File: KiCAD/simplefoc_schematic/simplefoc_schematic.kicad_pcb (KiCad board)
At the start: 2 copper layers, 51.9 x 74.3 mm, 67 parts, among them IC1 TMC6140-Trinamic, J1 Power Supply, J2 Motor Connector, J3 Sensor Connector, J5 Programming Port, J6 UART Port, J7 Conn_01x03, Q1 IRLR 2905, Q2 IRLR 2905, Q3 IRLR 2905, Q4 IRLR 2905, Q5 IRLR 2905, Q6 IRLR 2905, SW1 SW_Push, U2 STM32F101CBT6, Y1 8MHz

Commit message: Removed unused components and replaced some components with smaller ones
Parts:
- removed C21: 10uF/35V, Capacitor_SMD:CP_Elec_4x5.8
- removed C32: 100nF/35V, Capacitor_SMD:C_0603_1608Metric
- removed C33: 10uF/6.3V, Capacitor_SMD:C_0603_1608Metric
- removed D3: D_Schottky, Diode_SMD:D_SMA
- removed R13: 47k, Resistor_SMD:R_0603_1608Metric
- removed Y1: 8MHz, Crystal:Crystal_SMD_HC49-SD
- added U1: MC7805CDTG, Package_TO_SOT_SMD:TO-252-2, F.Cu at (254.9, 59.2)
- C12: value 100nF/35V -> 10uF/35V; moved to F.Cu
- C13: value 20pF/6V -> 10uF/35V; moved to F.Cu
- C14, C16: footprint Capacitor_SMD:CP_Elec_4x5.8 -> Capacitor_SMD:C_0603_1608Metric
- C18: value 20pF/6V -> 100nF/35V; moved to F.Cu
- C19: footprint Capacitor_SMD:CP_Elec_4x5.8 -> Capacitor_SMD:C_0603_1608Metric; moved to F.Cu
- C25, C26: value 10uF/6.3V -> 22uF/6.3V
- D1, D2: footprint Diode_SMD:D_SMA -> Additional_Components:DIODE_MSS1P4-M3_89A
- J7: value Conn_01x03 -> Servo
- R10: value 1mOhm/3W -> 0R; footprint Resistor_SMD:R_2512_6332Metric -> Resistor_SMD:R_0603_1608Metric; moved to F.Cu
- R12: value 47k -> 22k
- R7: value FBead -> 10k; footprint Resistor_SMD:R_0805_2012Metric -> Resistor_SMD:R_0603_1608Metric
- R8, R9: value 1mOhm/3W -> 10k; footprint Resistor_SMD:R_2512_6332Metric -> Resistor_SMD:R_0603_1608Metric
- moved R10 65.5 mm to (254.8, 26.8), turned to 0 degrees
- moved C19 33.2 mm to (262.9, 56.5), turned to 0 degrees
- moved C18 31.3 mm to (262.9, 59.0), turned to 0 degrees
- moved C13 20.6 mm to (278.5, 72.5), turned to 0 degrees
- moved C12 20.1 mm to (274.5, 72.5), turned to 0 degrees
- moved D1 10.2 mm to (247.0, 23.8)
- moved Q2 5.68 mm to (191.5, 80.2)
- moved Q4 5.68 mm to (191.5, 72.1)
- moved Q6 5.68 mm to (191.6, 87.4)
- moved Q1 5.68 mm to (203.6, 80.2)
- moved Q3 5.68 mm to (203.7, 87.5)
- moved Q5 5.68 mm to (203.6, 72.1)
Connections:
- C12 pad 1: +3.3V -> GND
- C12 pad 2: GND -> Net-(IC1-Pad33)
- C13 pad 1: GND -> +BATT
- C13 pad 2: Net-(C13-Pad2) -> GND
- C14 pad 1: Net-(C14-Pad1) -> +BATT
- C16 pad 1: GND -> +BATT
- C16 pad 2: +BATT -> GND
- C18 pad 2: Net-(C18-Pad2) -> +BATT
- C19 pad 1: GND -> +5V
- C19 pad 2: +BATT -> GND
- C3 pad 1: Net-(C3-Pad1) -> +3.3V
- C5 pad 1: Net-(C3-Pad1) -> +3.3V
- IC1 pad 10: Net-(C22-Pad2) -> Net-(IC1-Pad10)
- IC1 pad 22: CURRU -> unconnected-(IC1-Pad22)
- IC1 pad 23: CURRV -> unconnected-(IC1-Pad23)
- IC1 pad 25: CURRW -> unconnected-(IC1-Pad25)
- IC1 pad 26: SensU -> GND
- IC1 pad 27: SensV -> GND
- IC1 pad 28: SensW -> GND
- IC1 pad 29: DRV_STRENGTH -> unconnected-(IC1-Pad29)
- IC1 pad 30: GAIN -> unconnected-(IC1-Pad30)
- IC1 pad 33: Net-(C14-Pad1) -> Net-(IC1-Pad33)
- J3 pad 5: Thermo -> unconnected-(J3-Pad5)
- J3 pad 6: +5V -> +3.3V
- L1 pad 2: Net-(C22-Pad2) -> Net-(IC1-Pad10)
- Q4 pad 3: SensU -> GND
- Q5 pad 3: SensV -> GND
- Q6 pad 3: SensW -> GND
- R10 pad 1: SensW -> Net-(IC1-Pad10)
- R10 pad 2: GND -> Net-(C22-Pad2)
- R12 pad 1: BRAKE-0 -> Net-(IC1-Pad19)
- R12 pad 2: Net-(IC1-Pad19) -> +3.3V
- R7 pad 2: Net-(C3-Pad1) -> ENCA
- R8 pad 1: SensV -> +3.3V
- R8 pad 2: GND -> ENCB
- R9 pad 1: SensU -> +3.3V
- R9 pad 2: GND -> ENCC
- U2 pad 10: unconnected-(U2-Pad10) -> Servo
- U2 pad 11: HO1 -> unconnected-(U2-Pad11)
- U2 pad 12: LO1 -> unconnected-(U2-Pad12)
- U2 pad 13: HO2 -> DIAG
- U2 pad 14: LO2 -> unconnected-(U2-Pad14)
- U2 pad 15: HO3 -> ENABLE
- U2 pad 16: LO3 -> unconnected-(U2-Pad16)
- U2 pad 17: CURRW -> ENCC
- U2 pad 18: CURRU -> ENCB
- U2 pad 19: CURRV -> ENCA
- U2 pad 25: ENCA -> unconnected-(U2-Pad25)
- U2 pad 26: ENCB -> LO1
- U2 pad 27: ENCC -> LO2
- U2 pad 28: unconnected-(U2-Pad28) -> LO3
- U2 pad 29: unconnected-(U2-Pad29) -> HO1
- U2 pad 30: unconnected-(U2-Pad30) -> HO2
- U2 pad 31: unconnected-(U2-Pad31) -> HO3
- U2 pad 42: unconnected-(U2-Pad42) -> TX
- U2 pad 43: unconnected-(U2-Pad43) -> RX
- U2 pad 5: Net-(C13-Pad2) -> unconnected-(U2-Pad5)
- U2 pad 6: Net-(C18-Pad2) -> unconnected-(U2-Pad6)
- U2 pad 9: Net-(C3-Pad1) -> +3.3V

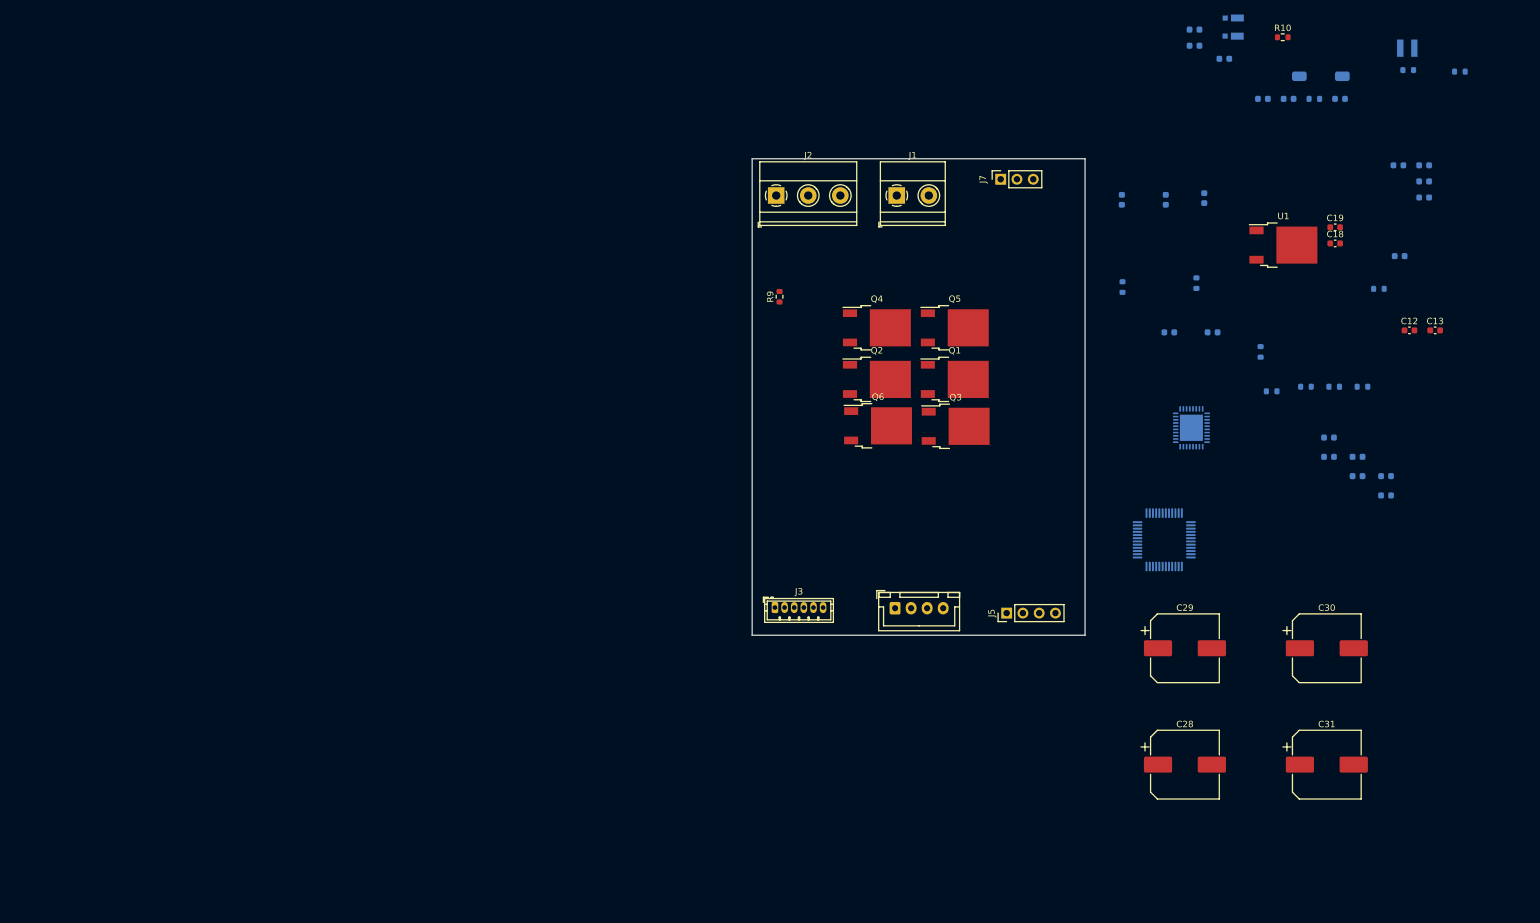
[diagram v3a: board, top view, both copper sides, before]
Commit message: Created first board layout for test board
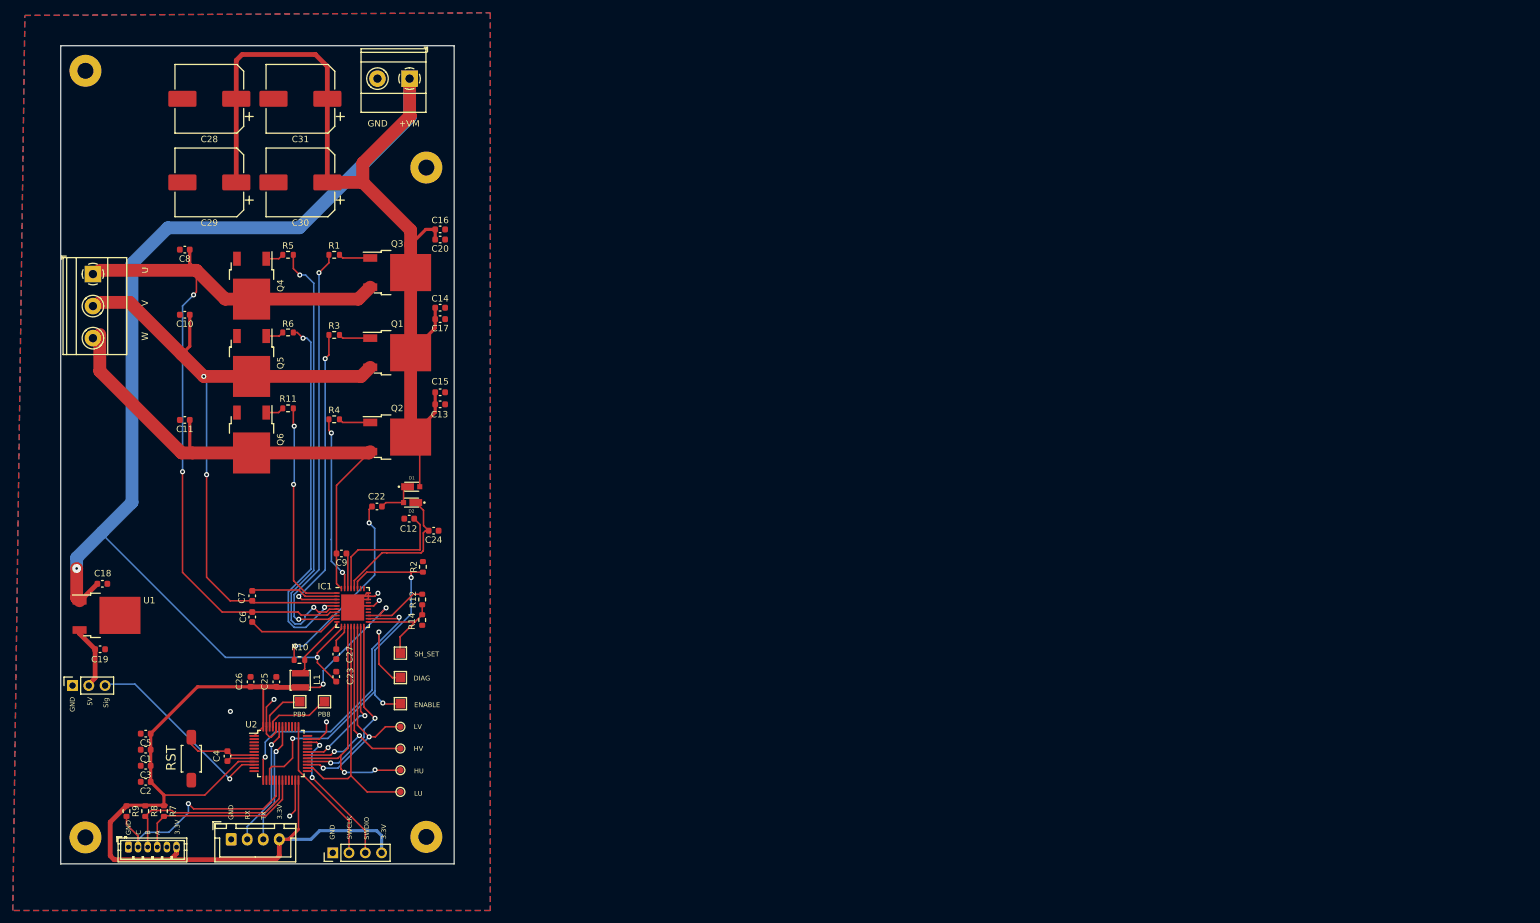
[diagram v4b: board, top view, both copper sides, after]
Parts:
- added H1: MountingHole_Pad, MountingHole:MountingHole_2.5mm_Pad, F.Cu at (121.2, 47.1)
- added H2: MountingHole_Pad, MountingHole:MountingHole_2.5mm_Pad, F.Cu at (68.0, 151.6)
- added H3: MountingHole_Pad, MountingHole:MountingHole_2.5mm_Pad, F.Cu at (68.0, 32.1)
- added H4: MountingHole_Pad, MountingHole:MountingHole_2.5mm_Pad, F.Cu at (121.2, 151.5)
- added TP1: TestPoint, TestPoint:TestPoint_Pad_1.5x1.5mm, F.Cu at (117.1, 122.9)
- added TP2: TestPoint, TestPoint:TestPoint_Pad_1.5x1.5mm, F.Cu at (117.1, 130.8)
- added TP3: TestPoint, TestPoint:TestPoint_Pad_D1.0mm, F.Cu at (117.1, 141.1)
- added TP4: TestPoint, TestPoint:TestPoint_Pad_1.5x1.5mm, F.Cu at (117.1, 126.7)
- added TP5: TestPoint, TestPoint:TestPoint_Pad_1.5x1.5mm, F.Cu at (101.4, 130.5)
- added TP6: TestPoint, TestPoint:TestPoint_Pad_1.5x1.5mm, F.Cu at (105.3, 130.5)
- added TP7: TestPoint, TestPoint:TestPoint_Pad_D1.0mm, F.Cu at (117.1, 144.5)
- added TP8: TestPoint, TestPoint:TestPoint_Pad_D1.0mm, F.Cu at (117.1, 137.8)
- added TP9: TestPoint, TestPoint:TestPoint_Pad_D1.0mm, F.Cu at (117.1, 134.4)
- C1, C10, C11, C14, C15, C16, C17, C2, C20, C22, C23, C24, C25, C26, C27, C3, C4, C5, C6, C7, C8, C9, D1, D2, IC1, L1, R1, R11, R12, R14, R2, R3, R4, R5, R6, R7, R8, SW1, U2: moved to F.Cu
- moved C5 216.2 mm to (77.4, 135.4)
- moved C2 212.1 mm to (77.4, 143.0)
- moved R8 209.0 mm to (77.3, 147.5), turned to -90 degrees
- moved SW1 205.8 mm to (84.5, 139.3), turned to 90 degrees
- moved C19 203.6 mm to (70.3, 122.3)
- moved C18 199.5 mm to (70.7, 112.1), turned to 180 degrees
- moved L1 198.8 mm to (101.5, 127.1), turned to 90 degrees
- moved C10 194.7 mm to (83.5, 70.1)
- moved C11 193.4 mm to (83.5, 86.5)
- moved C26 192.7 mm to (93.8, 127.4), turned to -90 degrees
- moved U1 192.4 mm to (71.3, 117.0)
- moved C31 190.8 mm to (101.5, 36.4), turned to 180 degrees
- moved R7 184.8 mm to (80.3, 147.5), turned to -90 degrees
- moved C28 184.2 mm to (87.3, 36.4), turned to 180 degrees
- moved R14 183.1 mm to (120.5, 117.7), turned to 90 degrees
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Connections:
- net Net-(IC1-Pad19) renamed SH_SET
- J1 pad 1: GND -> +BATT
- J1 pad 2: +BATT -> GND
- J2 pad 1: W -> U
- J2 pad 3: U -> W
- U2 pad 45: unconnected-(U2-Pad45) -> PB8
- U2 pad 46: unconnected-(U2-Pad46) -> PB9
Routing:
- net +BATT: track 0.00 -> 323.4 mm, vias 0 -> 2
- net +3.3V: track 0.00 -> 171.9 mm, vias 0 -> 2
- net U: track 0.00 -> 123.5 mm, vias 0 -> 2
- net V: track 0.00 -> 107.7 mm, vias 0 -> 2
- net W: track 0.00 -> 82.4 mm
- net LOUTU: track 0.00 -> 69.6 mm, vias 0 -> 2
- net HOUTU: track 0.00 -> 65.8 mm, vias 0 -> 2
- net ENABLE: track 0.00 -> 63.0 mm, vias 0 -> 3
- net LOUTV: track 0.00 -> 57.9 mm, vias 0 -> 2
- net DIAG: track 0.00 -> 56.2 mm, vias 0 -> 3
- net HOUTV: track 0.00 -> 48.9 mm, vias 0 -> 2
- net GND: track 0.00 -> 40.8 mm, vias 0 -> 6
- net LO1: track 0.00 -> 39.7 mm
- net HO1: track 0.00 -> 37.8 mm, vias 0 -> 2
- net LO2: track 0.00 -> 35.4 mm, vias 0 -> 2
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- added copper zone on B.Cu, net GND
- added copper zone on F.Cu, net GND
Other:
- board size 51.9 x 74.3 mm -> 61.4 x 127.6 mm
- board text added: "+VM"
- board text added: "3.3V"
- board text added: "5V"
- board text added: "A"
- board text added: "B"
- board text added: "C"
- board text added: "DIAG"
- board text added: "ENABLE"
- board text added: "GND"
- board text added: "HU"
- board text added: "HV"
- board text added: "LU"
- board text added: "LV"
- board text added: "PB8"
- board text added: "PB9"
- board text added: "RST"
- board text added: "RX"
- board text added: "SH_SET"
- board text added: "SWCLK"
- board text added: "SWDIO"
- board text added: "Sig"
- board text added: "TX"
- board text added: "U"
- board text added: "V"
- board text added: "W"

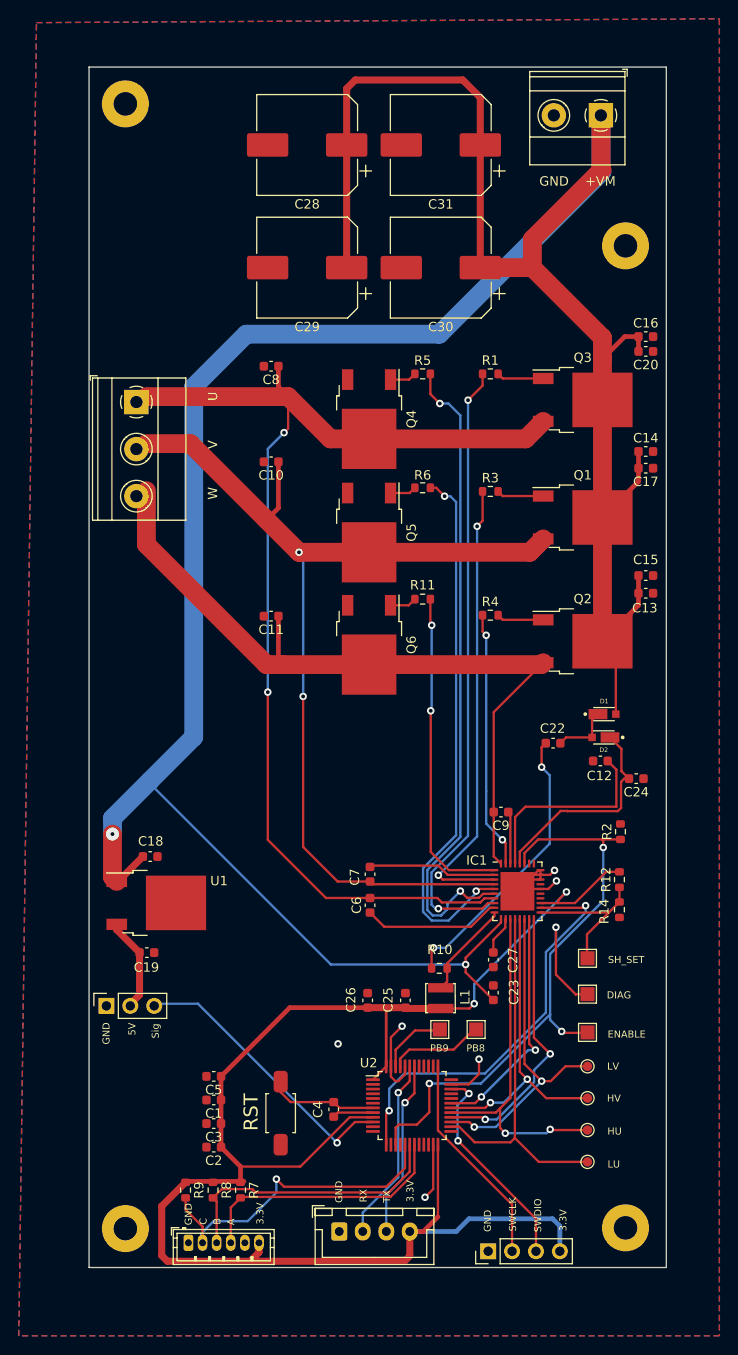
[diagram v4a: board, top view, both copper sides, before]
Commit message: Minor changes to power tracks
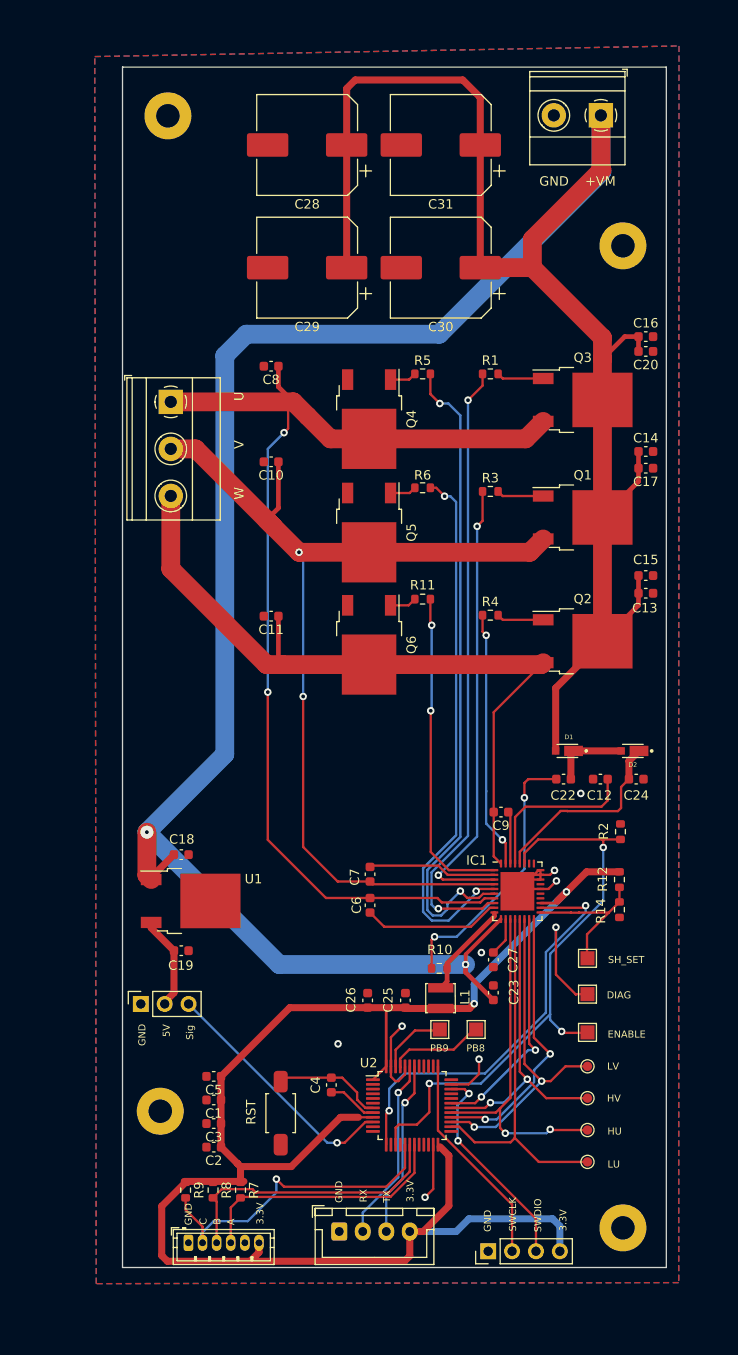
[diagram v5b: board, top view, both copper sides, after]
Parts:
- moved H2 13.0 mm to (71.7, 139.1)
- moved D1 5.52 mm to (115.0, 100.8), turned to 180 degrees
- moved H3 4.70 mm to (72.5, 33.3)
- moved C22 3.98 mm to (114.6, 103.8)
- moved C19 3.66 mm to (74.0, 122.1)
- moved J7 3.66 mm to (69.7, 127.7)
- moved U1 3.66 mm to (75.0, 116.8)
- moved J2 3.66 mm to (72.8, 63.7)
- moved D2 3.40 mm to (122.0, 100.8)
- moved C18 3.31 mm to (74.0, 111.9)
- moved C4 2.60 mm to (89.9, 136.3)
- moved C12 1.93 mm to (118.5, 103.8)
- moved H1 0.27 mm to (120.9, 47.1)
- moved H4 0.27 mm to (120.9, 151.5)
- moved C24 0.05 mm to (122.3, 103.8)
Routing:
- net Servo: track 30.4 -> 26.6 mm
- net Net-(IC1-Pad33): track 21.4 -> 17.8 mm
- net U: track 123.5 -> 120.7 mm
- net Net-(C24-Pad2): track 22.9 -> 20.8 mm
- net V: track 107.7 -> 105.9 mm
- net Net-(C22-Pad1): track 6.36 -> 8.17 mm
- net Net-(C22-Pad2): track 30.4 -> 28.7 mm
- net W: track 82.4 -> 80.8 mm
- net +BATT: track 323.4 -> 324.7 mm
- net GND: track 40.8 -> 41.8 mm, vias 6 -> 8
- net +3.3V: track 171.9 -> 171.2 mm
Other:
- board size 61.4 x 127.6 mm -> 57.8 x 127.6 mm

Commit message: First design of the final small PCB
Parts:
- removed C22: 100nF/35V, Capacitor_SMD:C_0603_1608Metric
- removed C28, C29, C31: 1000uF/25V, Capacitor_SMD:CP_Elec_10x14.3
- removed D1, D2: D_Schottky, Additional_Components:DIODE_MSS1P4-M3_89A
- removed R10: 0R, Resistor_SMD:R_0603_1608Metric
- removed TP1, TP2, TP4, TP5, TP6: TestPoint, TestPoint:TestPoint_Pad_1.5x1.5mm
- removed TP3, TP7, TP8, TP9: TestPoint, TestPoint:TestPoint_Pad_D1.0mm
- added G***: LOGO, LOGO, F.Cu at (103.3, 99.7)
- added G***: LOGO, LOGO, F.Cu at (114.7, 103.5)
- C1, C10, C11, C12, C13, C14, C15, C16, C17, C18, C19, C2, C20, C23, C24, C25, C26, C27, C3, C4, C5, C6, C7, C8, C9, IC1, L1, R1, R11, R12, R14, R2, R3, R4, R5, R6, R7, R8, R9, U2: moved to B.Cu
- C30: value 1000uF/25V -> 220uF/25V; footprint Capacitor_SMD:CP_Elec_10x14.3 -> Capacitor_SMD:CP_Elec_8x10
- H1, H2, H3, H4: footprint MountingHole:MountingHole_2.5mm_Pad -> MountingHole:MountingHole_2.2mm_M2_DIN965_Pad
- moved H4 89.4 mm to (123.6, 62.2)
- moved J7 78.7 mm to (112.7, 61.8)
- moved H2 77.1 mm to (76.1, 62.2)
- moved J3 74.9 mm to (80.9, 78.5), turned to -90 degrees
- moved H3 73.3 mm to (76.1, 106.6)
- moved R9 68.2 mm to (83.7, 80.0), turned to 180 degrees
- moved R8 66.3 mm to (83.7, 81.6), turned to 180 degrees
- moved C19 66.0 mm to (113.1, 68.9)
- moved R7 64.5 mm to (83.7, 83.1), turned to 180 degrees
- moved U1 64.3 mm to (116.3, 67.5)
- moved C18 61.6 mm to (113.1, 64.3)
- moved J6 61.4 mm to (82.1, 91.1), turned to -90 degrees
- moved H1 59.5 mm to (123.6, 106.6)
- moved J5 54.0 mm to (87.6, 103.4), turned to -90 degrees
- moved SW1 53.0 mm to (104.5, 90.3), turned to 180 degrees
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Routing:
- net +BATT: track 324.7 -> 80.2 mm, vias 2 -> 5
- net U: track 120.7 -> 70.5 mm
- net ENABLE: track 63.0 -> 16.1 mm, vias 3 -> 0
- net V: track 105.9 -> 60.1 mm
- net DIAG: track 56.2 -> 18.8 mm, vias 3 -> 0
- net +3.3V: track 171.2 -> 134.8 mm, vias 2 -> 3
- net Servo: track 26.6 -> 62.9 mm, vias 1 -> 2
- net Net-(C22-Pad2): track 28.7 -> 0.00 mm, vias 2 -> 0
- net W: track 80.8 -> 54.2 mm, vias 0 -> 2
- net LOUTU: track 69.6 -> 50.7 mm, vias 2 -> 0
- net GND: track 41.8 -> 23.3 mm, vias 8 -> 27
- net Net-(C24-Pad2): track 20.8 -> 2.66 mm
- net HOUTV: track 48.9 -> 31.1 mm, vias 2 -> 0
- net HOUTU: track 65.8 -> 48.4 mm, vias 2 -> 0
- net Net-(C12-Pad2): track 17.8 -> 2.19 mm
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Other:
- board size 57.8 x 127.6 mm -> 52.3 x 49.1 mm
- board text added: "Car Controller v1.0"
- board text added: "Reset"
- board text added: "S"
- board text removed: "5V"
- board text removed: "DIAG"
- board text removed: "ENABLE"
- board text removed: "HU"
- board text removed: "HV"
- board text removed: "LU"
- board text removed: "LV"
- board text removed: "PB8"
- board text removed: "PB9"
- board text removed: "RST"
- board text removed: "SH_SET"
- board text removed: "Sig"
